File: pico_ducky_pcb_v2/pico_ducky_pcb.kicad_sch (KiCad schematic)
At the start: 32 parts, among them J1 USB_A, J3 Conn_ARM_JTAG_SWD_10, SW1 R-667799, SW2 R-667799, U1 AP2127K-3.3, U2 W25Q32JVZP, U3 RP2040, Y1 Crystal_GND24

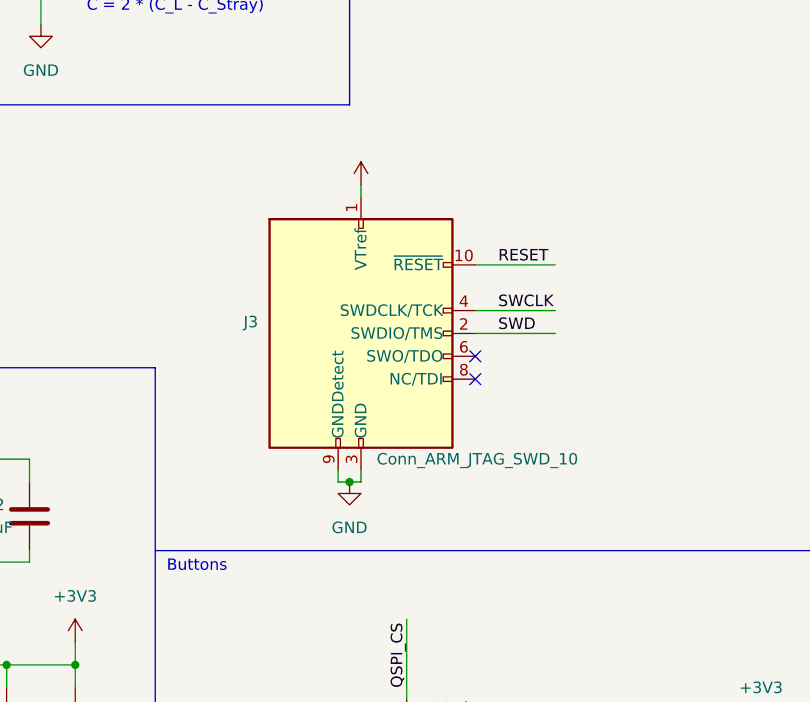
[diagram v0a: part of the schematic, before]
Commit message: start stripping v1 features
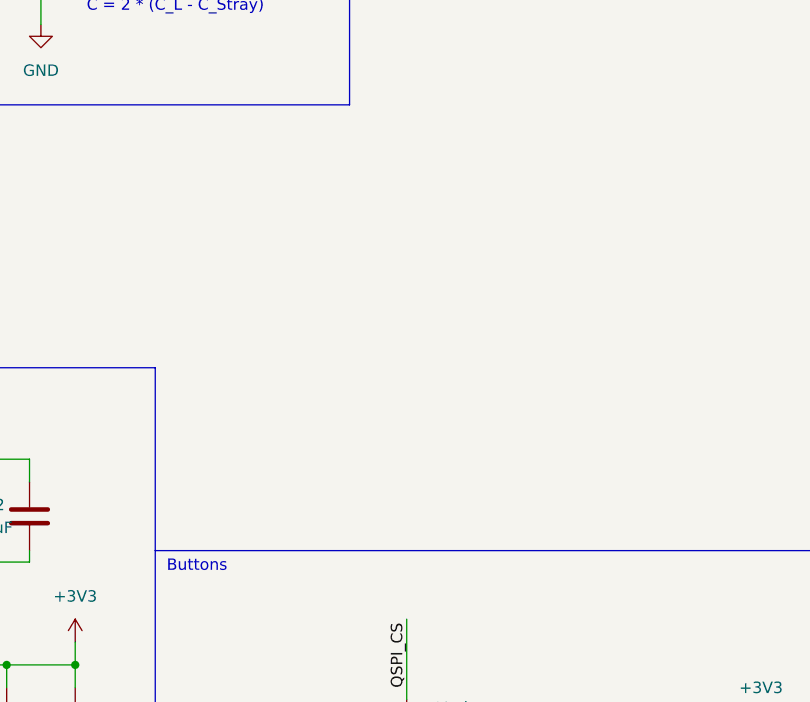
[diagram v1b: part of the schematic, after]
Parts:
- removed J3: Conn_ARM_JTAG_SWD_10, Connector_PinHeader_1.27mm:PinHeader_2x05_P1.27mm_Vertical, symbol Connector:Conn_ARM_JTAG_SWD_10
- U2: footprint 8-UFDFN:W25Q80DVUXIE TR -> Package_SON:WSON-8-1EP_6x5mm_P1.27mm_EP3.4x4.3mm
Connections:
- no-connect marks 31 -> 29

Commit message: route out most of the pcb
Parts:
- removed D2: NSR0320, Diode_SMD:D_SOD-323, symbol Diode:NSR0320
- removed R4: 1k, Resistor_SMD:R_0402_1005Metric, symbol Device:R_Small
- removed U1: AP2127K-3.3, Package_TO_SOT_SMD:SOT-23-5, symbol Regulator_Linear:AP2127K-3.3
- added JP1: SolderJumper_2_Open, Jumper:SolderJumper-2_P1.3mm_Open_RoundedPad1.0x1.5mm, symbol Jumper:SolderJumper_2_Open
- added R1: 10k, Resistor_SMD:R_0402_1005Metric, symbol Device:R_Small
- added U1: MIC5504-3.3YM5, Package_DFN_QFN:UDFN-4-1EP_1x1mm_P0.65mm_EP0.48x0.48mm, symbol Regulator_Linear:MIC5504-3.3YM5
- R6, R7: footprint Resistor_SMD:R_0402_1005Metric -> Resistor_SMD:R_0201_0603Metric
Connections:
- net +3V3: now also R1.1, U1.5 (VOUT)
- net +5V: now also U1.1 (VIN), U1.3 (EN)
- net GND: now also JP1.1 (A), U1.2 (GND)
- net QSPI_CS: now also JP1.2 (B)
- net USB_BOOT: no longer SW1.B1, SW1.B2, SW1.B3
- net X_IN: now also Y1.1; no longer Y1.3
- net at C16.2, R3.1: now also Y1.3; no longer Y1.1
- new net SAFE_BOOT: R1.2, SW1.B1, SW1.B2, SW1.B3
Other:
- moved on the sheet: Y1
